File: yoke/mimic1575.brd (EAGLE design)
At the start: 165.1 x 114.3 mm, 71 parts, among them P1 44PINEDGE, P2 20, Q1 2N3906, Q10 KSP05TA, Q11 2N3904, Q12 2N3904, Q13 2N3904, Q14 2N3904, Q15 2N3904, Q16 2N2222A, Q17 2N3904, Q18 2N3904, Q19 2N3904, Q2 2N3906, Q20 2N2222A, Q3 2N3906, Q4 2N2907, Q5 2N3906, Q6 2N3906, Q7 KSP05TA, Q8 2N3904, Q9 2N3906

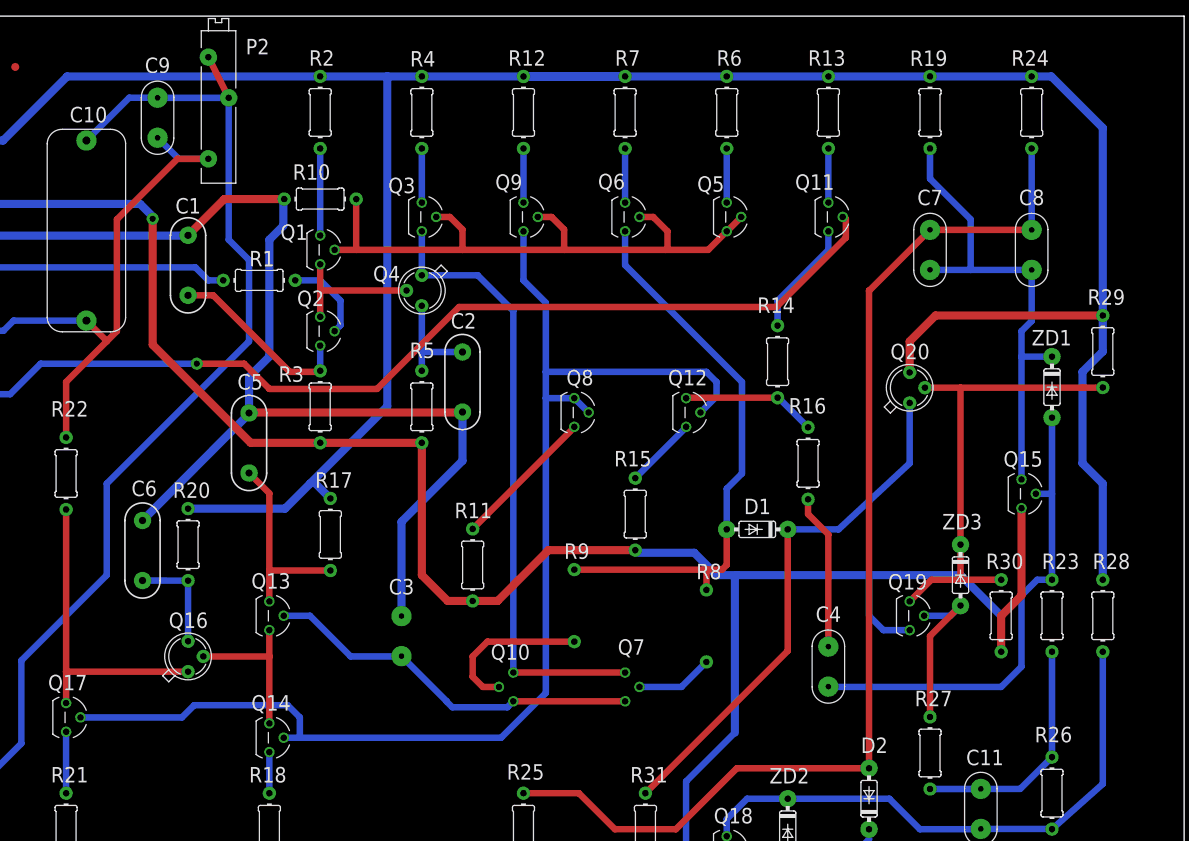
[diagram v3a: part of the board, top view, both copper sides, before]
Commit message: preamplifier card being routed
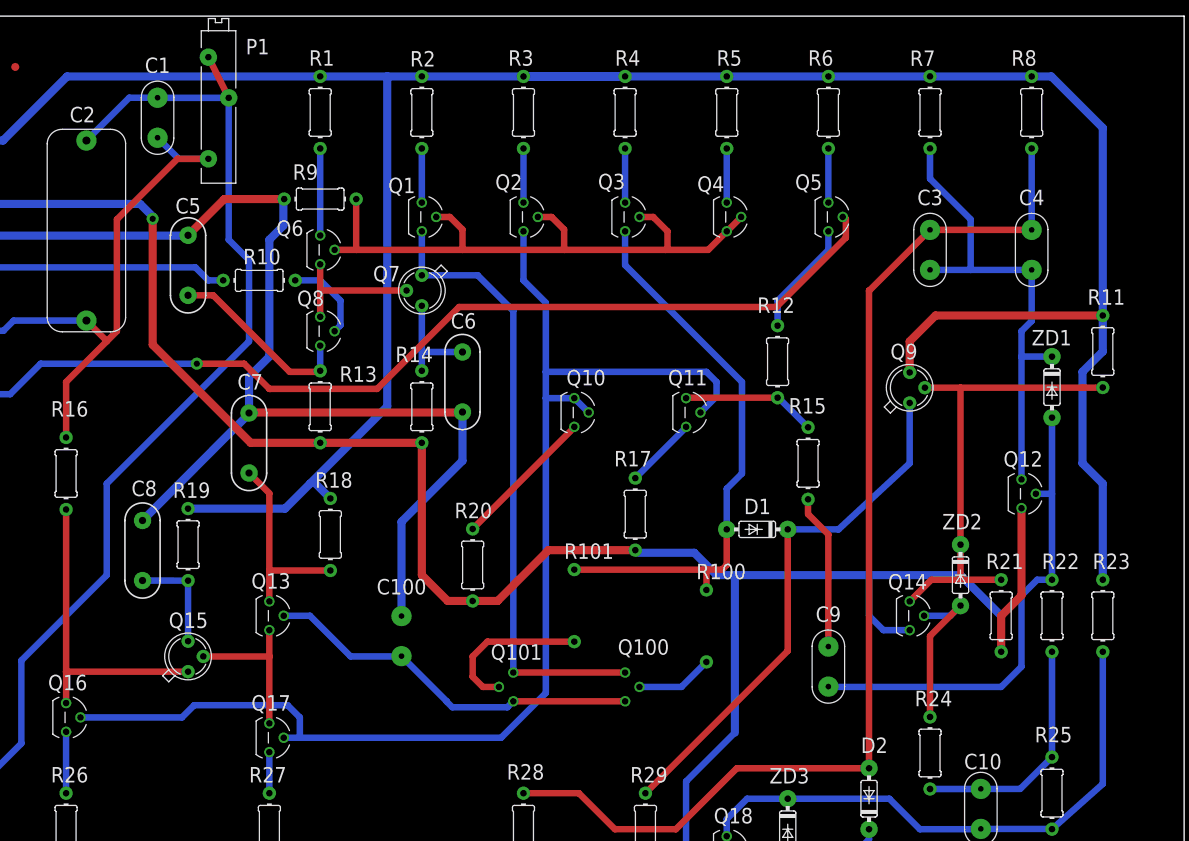
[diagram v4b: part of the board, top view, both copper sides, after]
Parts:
- removed C11: 56pF, keiths:5MM_TH
- removed Q19: 2N3904, keiths:TO92
- removed Q20: 2N2222A, keiths:TO18
- removed R30: 10K, keiths:R_QUARTERWATT
- removed R31: 560, keiths:R_QUARTERWATT
- added C100: 120pF, keiths:5MM_TH
- added Q100, Q101: KSP05TA, keiths:TO92
- added R100, R101: 680, keiths:R_QUARTERWATT
- C1: value 0.022uF -> 0.1uF; device keiths:CAP-ZERO-PT-ZERO-22UF-250V-FILM -> keiths:5MM_TH
- C10: value 3.3 UF -> 56pF; device keiths:ECW-FD2W335K -> keiths:5MM_TH
- C2: value 0.022 uF -> 3.3 UF; device keiths:CAP-ZERO-PT-ZERO-22UF-250V-FILM -> keiths:ECW-FD2W335K
- C3: value 120pF -> 680pF
- C4: value 0.001uF -> 330pF
- C5: value 0.022 uF -> 0.022uF
- C6: value 0.022uF -> 0.022 uF
- C7: value 680pF -> 0.022 uF; device keiths:5MM_TH -> keiths:CAP-ZERO-PT-ZERO-22UF-250V-FILM
- C8: value 330pF -> 0.022uF; device keiths:5MM_TH -> keiths:CAP-ZERO-PT-ZERO-22UF-250V-FILM
- C9: value 0.1uF -> 0.001uF
- P1: value 44PINEDGE -> 20; device keiths:44PINEDGE -> keiths:3006P
- P2: value 20 -> 44PINEDGE; device keiths:3006P -> keiths:44PINEDGE
- Q10: value KSP05TA -> 2N3904
- Q15: value 2N3904 -> 2N2222A; device keiths:TO92 -> keiths:TO18
- Q16: value 2N2222A -> 2N3904; device keiths:TO18 -> keiths:TO92
- Q4: value 2N2907 -> 2N3906; device keiths:TO18 -> keiths:TO92
- Q5: value 2N3906 -> 2N3904
- Q7: value KSP05TA -> 2N2907; device keiths:TO92 -> keiths:TO18
- Q8: value 2N3904 -> 2N3906
- Q9: value 2N3906 -> 2N2222A; device keiths:TO92 -> keiths:TO18
- R10, R22: value 1K -> 120
- R11, R7: value 27 -> 560
- R12: value 27 -> 1.5K
- R13: value 470 -> 560
- R14: value 1.5K -> 120
- R15: value 27 -> 220
- R16: value 220 -> 1K
- R17: value 1.5K -> 27
- R18: value 120 -> 1.5K
- R19: value 560 -> 330
- R2, R5: value 120 -> 27
- R20: value 330 -> 27
- R21: value 27 -> 10K
- R23: value 120 -> 1K
- R24: value 560 -> 120
- R25: value 560 -> 1K
- R26: value 1K -> 27
- R28: value 1K -> 560
- R3: value 560 -> 27
- R6: value 27 -> 470
- R8: value 680 -> 560
- R9: value 680 -> 1K
- moved C10 133.1 mm to (139.7, 15.2), turned to 270 degrees
- moved R22 124.5 mm to (148.6, 39.4)
- moved R26 123.3 mm to (25.4, 12.7)
- moved R21 119.8 mm to (142.2, 39.4)
- moved C8 117.3 mm to (35.0, 47.5), turned to 270 degrees
- moved C9 108.3 mm to (120.7, 33.0), turned to 270 degrees
- moved R19 107.3 mm to (40.6, 48.3)
- moved Q15 106.1 mm to (40.6, 34.3), turned to 270 degrees
- moved R16 92.7 mm to (25.4, 57.1), turned to 270 degrees
- moved C7 88.4 mm to (48.3, 61.0), turned to 270 degrees
- moved R11 83.1 mm to (154.9, 72.4)
- moved R27 83.1 mm to (50.8, 12.7)
- moved R29 82.6 mm to (97.8, 12.7)
- moved C3 81.8 mm to (133.3, 85.1), flipped to the top
- moved Q14 81.4 mm to (130.8, 39.4)
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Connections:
- removed net N$16 (its old number): Q6.3, R7.1
- removed net N$38 (its old number): Q11.3, R13.1
- new net N$10: Q4.3, R5.1
- new net N$26: Q6.3, R1.1
- net +10V: now also P2.A, Q9.3, R1.2, R11.2, R18.2, R23.2, R3.2, R5.2, R8.2; no longer P1.A, Q20.3, R12.2, R13.2, R17.2, R20.2, R24.2, R28.2, R29.2
- net -15V: now also P2.C, Q12.1, Q14.1, R13.1, R14.1, R17.1, R20.1, R26.1, R27.1, R28.1, R29.1; no longer P1.C, Q15.1, Q19.1, R11.1, R15.1, R18.1, R25.1, R3.1, R30.1, R31.1, R5.1
- net E_IN: now also P2.E, R10.2; no longer P1.E, R1.2
- net GND: now also C100.2, C7.1, C8.1, P2.D, R9.1; no longer C1.1, C2.1, C3.2, P1.D, R10.1
- net H_IN: now also C1.1, C2.1, P1.1, P2.H, R16.1; no longer C10.1, C9.1, P1.H, P2.1, R22.1
- net K_IN: now also P2.K, Q5.2; no longer P1.K, Q11.2
- net N$1: now also C9.1, R15.1; no longer C4.1, R16.1
- net N$11: now also Q14.3, Q9.2, R11.1, R21.2, ZD2.C; no longer Q19.3, Q20.2, R29.1, R30.2, ZD3.C
- net N$12: now also Q14.2, R24.2, ZD2.A; no longer Q19.2, R27.2, ZD3.A
- net N$13: now also C6.2, Q7.3, R14.2; no longer C2.2, Q4.3, R5.2
- net N$14: now also Q10.2, Q10.3, Q11.2, Q16.2, Q2.1; no longer Q12.2, Q14.2, Q8.2, Q8.3, Q9.1
- net N$15: now also Q1.1, Q100.1, Q101.3; no longer Q10.3, Q3.1, Q4.1
- net N$17: now also Q100.2, R100.1; no longer Q7.2, R8.1
- net N$18: now also Q17.1, R27.2; no longer Q14.1, R18.2
- net N$19: now also Q101.2, R101.1; no longer Q10.2, R9.1
- net N$2: now also C3.1, C4.1, Q12.3, R7.1; no longer C7.1, C8.1, Q15.3, R19.1
- net N$20: now also C100.1, Q100.3, Q101.1; no longer C3.1, Q10.1, Q7.3
- net N$21: now also Q2.2, Q4.1, Q4.2, R9.2; no longer Q5.1, Q5.2, Q9.2, R10.2
- net N$22: now also Q15.2, Q17.3; no longer Q14.3, Q16.2
- net N$23: now also Q3.1, R100.2, R101.2; no longer Q6.1, R8.2, R9.2
- net N$24: now also Q2.3, R3.1; no longer Q9.3, R12.1
- net N$25: now also Q8.2, R10.1; no longer Q2.2, R1.1
- net N$27: now also C7.2, R18.1; no longer C5.2, R17.1
- net N$28: now also Q11.1, R17.2; no longer Q12.1, R15.2
- net N$3: now also C9.2, Q12.2, R22.1; no longer C4.2, Q15.2, R23.1
- net N$30: now also Q6.1, Q7.2, Q8.3; no longer Q1.1, Q2.3, Q4.2
- net N$31: now also C5.2, Q8.1, R13.2; no longer C1.2, Q2.1, R3.2
- net N$34: now also Q11.3, R12.1, R15.2; no longer Q12.3, R14.1, R16.2
- net N$36: now also Q16.1, R26.2; no longer Q17.1, R21.2
- net N$37: now also Q5.1, R12.2; no longer Q11.1, R14.2
- net N$39: now also Q15.1, Q16.3, R16.2; no longer Q16.1, Q17.3, R22.2
- net N$4: now also C10.1, R22.2, R24.1, R25.2; no longer C11.1, R23.2, R26.2, R27.1
- net N$40: now also C8.2, Q15.3, R19.1; no longer C6.2, Q16.3, R20.1
- net N$5: now also C10.2, R23.1, R25.1, ZD3.C; no longer C11.2, R26.1, R28.1, ZD2.C
- net N$6: now also Q9.1, R29.2; no longer Q20.1, R31.2
- net N$7: now also Q10.1, R20.2; no longer Q8.1, R11.2
- net N$8: now also ZD3.A; no longer ZD2.A
- net N$9: now also C3.2, C4.2, R28.2, R8.1; no longer C7.2, C8.2, R24.1, R25.2
- net Z_OUT: now also C1.2, C2.2, P1.2, P1.3, P2.Z; no longer C10.2, C9.2, P1.Z, P2.2, P2.3
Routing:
- net N$26: track 0.00 -> 10.9 mm
- net N$38 (its old number): track 6.76 -> 0.00 mm
- net N$16 (its old number): track 6.76 -> 0.00 mm
- net N$10: track 0.00 -> 6.76 mm
- net N$33: track 10.9 -> 6.76 mm

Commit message: added logo
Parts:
- moved U$1 17.8 mm to (36.8, 108.0)
- moved C10 10.9 mm to (143.5, 25.4), turned to 90 degrees
- moved R25 10.4 mm to (154.9, 25.4), turned to 270 degrees
- moved R26 7.42 mm to (20.8, 18.5)
- moved R27 7.42 mm to (46.2, 18.5)
- moved R28 5.84 mm to (82.5, 18.5)
- moved R29 5.84 mm to (97.8, 18.5)
- moved C1 5.34 mm to (37.1, 96.3)
- moved Q17 2.54 mm to (50.8, 26.7)
- moved R17 2.54 mm to (96.5, 54.6)
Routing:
- net N$4: track 30.1 -> 51.8 mm
- net N$14: track 157.7 -> 172.9 mm
- net N$5: track 70.5 -> 60.7 mm
- net -15V: track 338.9 -> 346.0 mm
- net H_IN: track 79.2 -> 73.1 mm
- net N$22: track 19.9 -> 17.4 mm
- net N$6: track 66.4 -> 63.9 mm
- net N$9: track 141.6 -> 139.1 mm
- net N$36: track 7.67 -> 5.33 mm
- net Z_OUT: track 137.4 -> 135.2 mm
- net N$28: track 9.03 -> 7.95 mm
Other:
- board text added: "board type 1575 / follow hold"
